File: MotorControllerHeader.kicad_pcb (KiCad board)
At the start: 2 copper layers, 20 parts, among them J1 Conn_01x02_Pin, J10 Conn_01x02_Socket, J11 Conn_01x02_Pin, J12 Conn_01x02_Socket, J13 Conn_01x02_Pin, J14 Conn_01x02_Socket, J15 Conn_01x02_Pin, J16 Conn_01x02_Socket, J19 Conn_02x04_Odd_Even, J2 Conn_01x02_Socket, J20 Conn_02x04_Odd_Even, J21 Conn_02x04_Odd_Even, J22 Conn_02x04_Odd_Even, J3 Conn_01x02_Pin, J4 Conn_01x02_Socket, J5 Conn_01x02_Pin, J6 Conn_01x02_Socket, J7 Conn_01x02_Pin, J8 Conn_01x02_Socket, J9 Conn_01x02_Pin

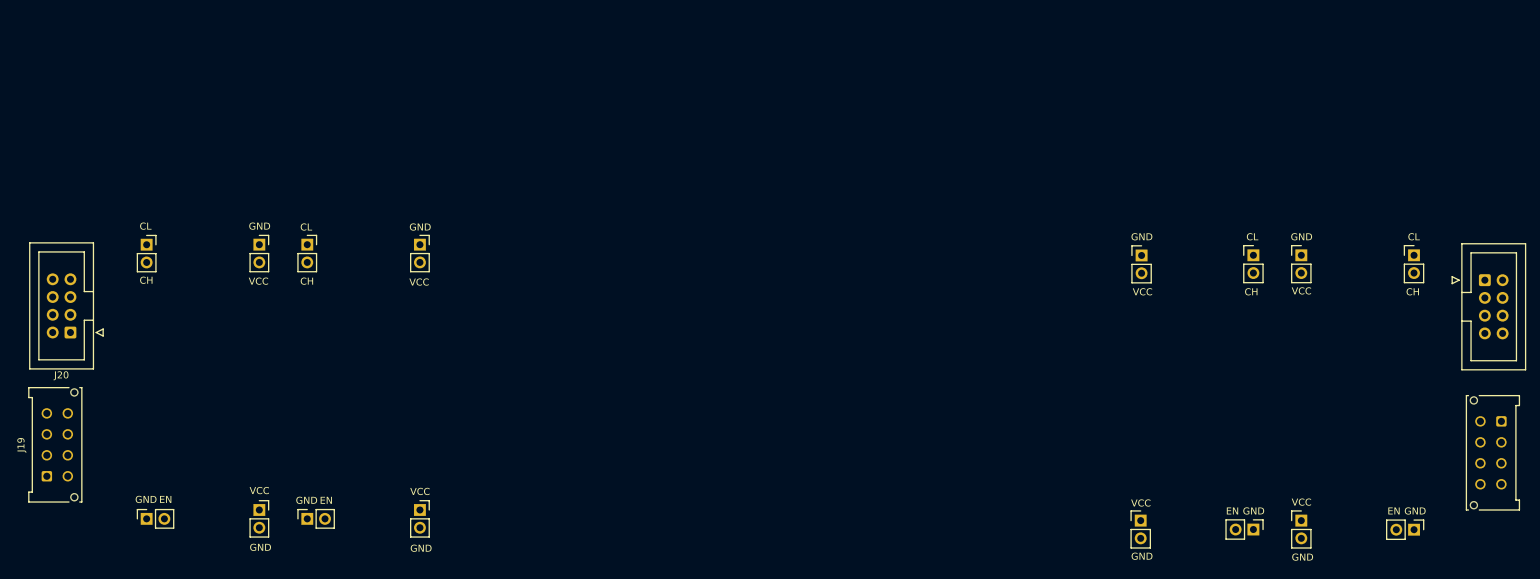
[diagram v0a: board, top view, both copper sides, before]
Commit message: Replanned Project: Removed ribbon cable; added female connectors on top and male connectors on bottom
Excludes KiCad backups, autosaves, lock files and .kicad_prl via .gitignore.
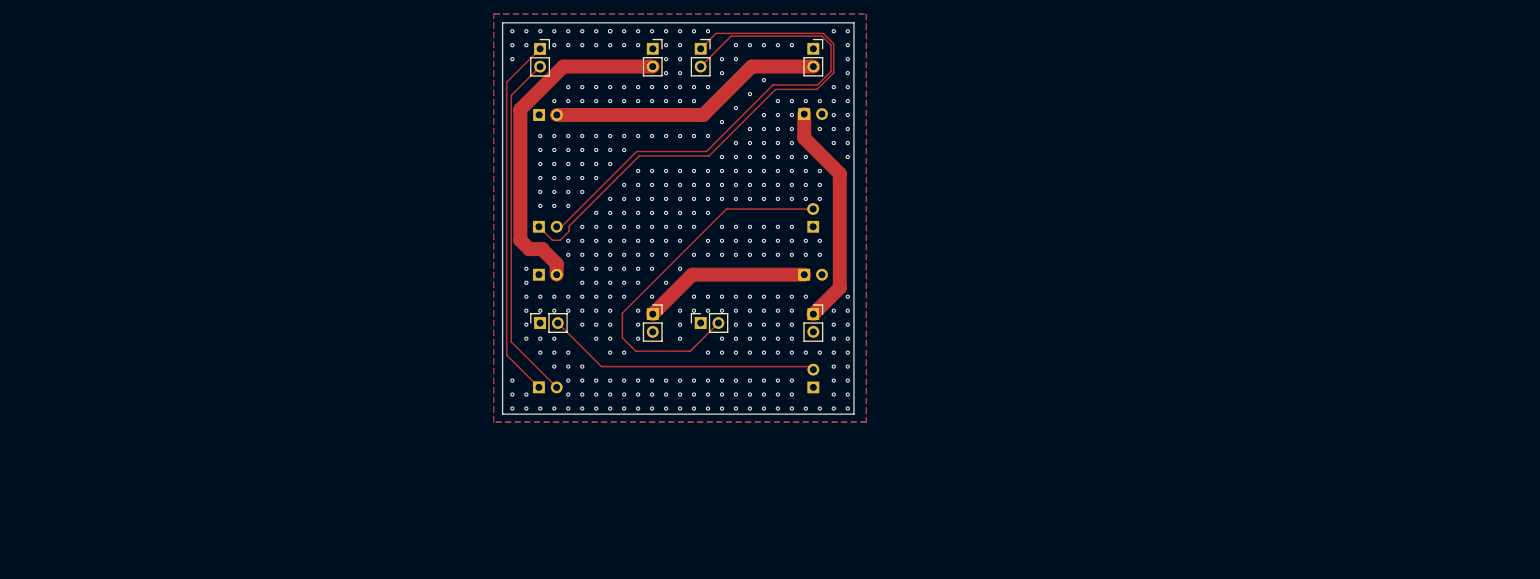
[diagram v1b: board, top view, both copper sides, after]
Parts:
- removed J19, J22: Conn_02x04_Odd_Even, Connector_Molex:Molex_Micro-Fit_3.0_43045-0812_2x04_P3.00mm_Vertical
- removed J20, J21: Conn_02x04_Odd_Even, Connector_IDC:IDC-Header_2x04_P2.54mm_Vertical
- J1, J11, J13, J15, J3, J5, J7, J9: moved to B.Cu
- moved J1 126.7 mm to (106.8, 103.0), turned to -90 degrees
- moved J3 109.2 mm to (106.8, 86.8), turned to -90 degrees
- moved J5 102.3 mm to (106.8, 80.0), turned to -90 degrees
- moved J7 88.5 mm to (106.8, 64.0), turned to -90 degrees
- moved J9 88.4 mm to (146.1, 103.0), turned to 0 degrees
- moved J11 79.4 mm to (144.8, 86.8), turned to -90 degrees
- moved J13 76.5 mm to (146.1, 80.0), turned to 0 degrees
- moved J15 75.5 mm to (144.8, 63.9), turned to -90 degrees
- moved J12 62.9 mm to (123.1, 92.5)
- moved J16 62.9 mm to (146.1, 92.5)
- moved J4 62.9 mm to (123.1, 54.5)
- moved J8 62.9 mm to (146.1, 54.5)
- moved J10 62.9 mm to (107.0, 93.8)
- moved J14 62.9 mm to (129.9, 93.8)
- moved J2 62.9 mm to (107.0, 54.5)
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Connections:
- J10 pad 1: /1GND3 -> /GND
- J11 pad 2: /1GND2 -> /GND
- J12 pad 2: /1GND2 -> /GND
- J13 pad 1: /2GND3 -> /GND
- J14 pad 1: /2GND3 -> /GND
- J15 pad 2: /2GND2 -> /GND
- J16 pad 2: /2GND2 -> /GND
- J3 pad 1: /1GND1 -> /GND
- J4 pad 1: /1GND1 -> /GND
- J7 pad 1: /2GND1 -> /GND
- J8 pad 1: /2GND1 -> /GND
- J9 pad 1: /1GND3 -> /GND
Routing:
- net /2CL: track 0.00 -> 78.1 mm
- net /2CH: track 0.00 -> 73.2 mm
- net /2EN: track 0.00 -> 53.2 mm
- net /1CL: track 0.00 -> 52.3 mm
- net /1CH: track 0.00 -> 50.3 mm
- net /1VCC1: track 0.00 -> 48.4 mm
- net /2VCC1: track 0.00 -> 39.6 mm
- net /1EN: track 0.00 -> 39.3 mm
- net /2VCC2: track 0.00 -> 32.3 mm
- net /1VCC2: track 0.00 -> 24.0 mm
- net /GND: vias 0 -> 417
- added copper zone on B.Cu, net /GND
- added copper zone on F.Cu, net /GND
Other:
- board outline added: 50.3 x 56 mm
- board text removed: "CH"
- board text removed: "CL"
- board text removed: "EN"
- board text removed: "GND"
- board text removed: "VCC"

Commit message: Finish board layout, add 3D STEP export and README screenshot
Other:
- board text added: "CH"
- board text added: "CL"
- board text added: "EN"
- board text added: "GND"
- board text added: "VCC"

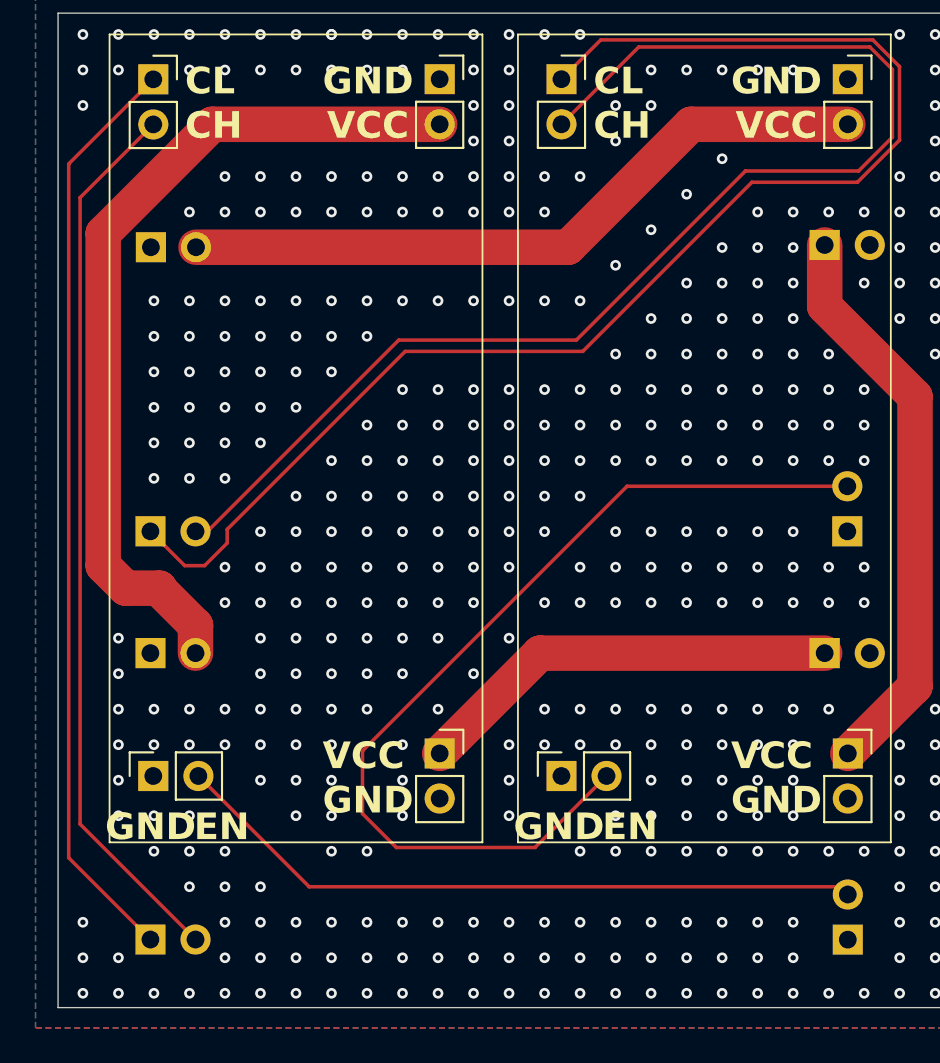
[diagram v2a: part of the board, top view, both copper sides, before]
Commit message: Update board layout, STEP export and production files
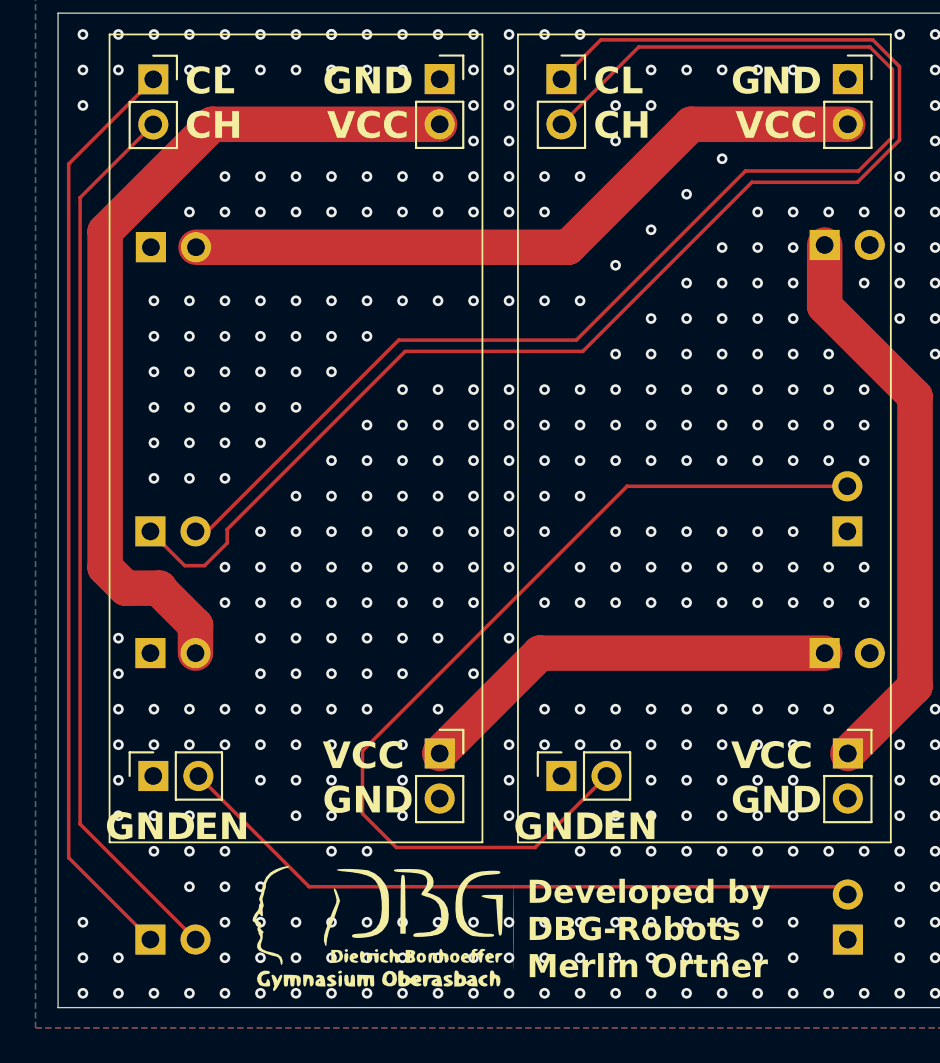
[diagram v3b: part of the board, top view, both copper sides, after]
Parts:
- added G***: LOGO, LOGO, F.Cu at (119.8, 102.2)
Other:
- board text added: "Developed by DBG-Robots Merlin Ortner"
